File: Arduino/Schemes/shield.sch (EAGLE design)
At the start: 10 parts

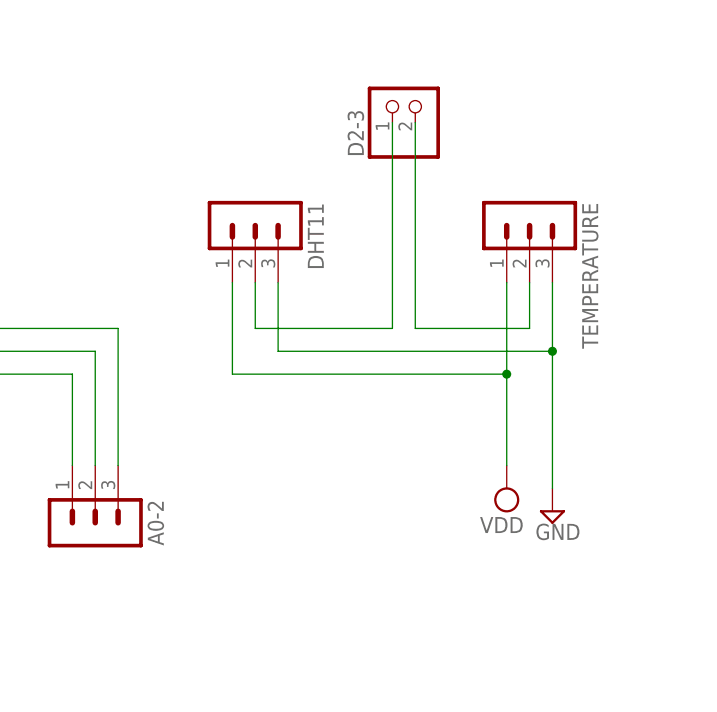
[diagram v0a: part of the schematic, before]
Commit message: relay board's scheme, shield with optional DHTxx
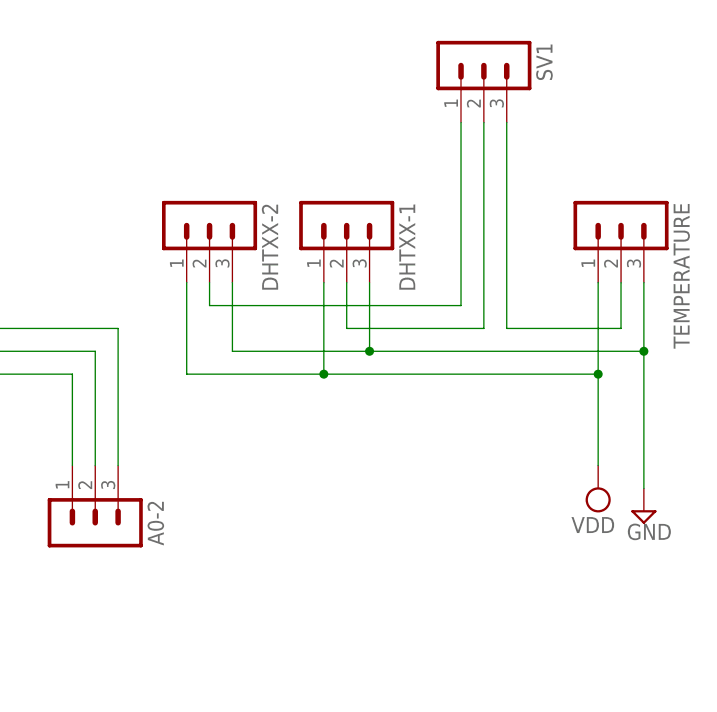
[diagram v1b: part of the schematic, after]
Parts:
- removed D2-3: (no value), pinhead:PINHD-1X2
- removed DHT11: (no value), con-lstb:MA03-1
- added DHTXX-1, DHTXX-2, SV1: (no value), con-lstb:MA03-1
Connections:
- new net N$9: DHTXX-2.2, SV1.1
- net GND: now also DHTXX-1.3, DHTXX-2.3; no longer DHT11.3
- net N$1: now also DHTXX-1.2, SV1.2; no longer D2-3.1, DHT11.2
- net N$2: now also SV1.3; no longer D2-3.2
- net VDD: now also DHTXX-1.1, DHTXX-2.1; no longer DHT11.1
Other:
- moved on the sheet: TEMPERATURE
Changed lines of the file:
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@@
 <part name="LIGHT" library="con-lstb" deviceset="MA03-1" device=""/>
 <part name="TEMPERATURE" library="con-lstb" deviceset="MA03-1" device=""/>
-<part name="DHT11" library="con-lstb" deviceset="MA03-1" device=""/>
+<part name="DHTXX-1" library="con-lstb" deviceset="MA03-1" device=""/>
 <part name="A0-2" library="con-lstb" deviceset="MA03-1" device=""/>
 <part name="5V-GND" library="pinhead" deviceset="PINHD-1X2" device=""/>
-<part name="D2-3" library="pinhead" deviceset="PINHD-1X2" device=""/>
 <part name="SUPPLY1" library="supply2" deviceset="GND" device=""/>
 <part name="SUPPLY2" library="supply2" deviceset="VDD" device=""/>
@@
 <part name="D8-10" library="con-lstb" deviceset="MA03-1" device=""/>
 <part name="RELAYS" library="con-lstb" deviceset="MA05-1" device=""/>
+<part name="SV1" library="con-lstb" deviceset="MA03-1" device=""/>
+<part name="DHTXX-2" library="con-lstb" deviceset="MA03-1" device=""/>
 </parts>
 <sheets>
@@
 <instance part="HUMIDITY2" gate="G$1" x="43.18" y="43.18" rot="R270"/>
 <instance part="LIGHT" gate="G$1" x="63.5" y="43.18" rot="R270"/>
-<instance part="TEMPERATURE" gate="G$1" x="139.7" y="40.64" rot="R270"/>
-<instance part="DHT11" gate="G$1" x="109.22" y="40.64" rot="R270"/>
+<instance part="TEMPERATURE" gate="G$1" x="149.86" y="40.64" rot="R270"/>
+<instance part="DHTXX-1" gate="G$1" x="119.38" y="40.64" rot="R270"/>
 <instance part="A0-2" gate="G$1" x="91.44" y="5.08" rot="MR90"/>
 <instance part="5V-GND" gate="G$1" x="25.4" y="-20.32" rot="R270"/>
-<instance part="D2-3" gate="G$1" x="127" y="53.34" rot="R90"/>
 <instance part="SUPPLY1" gate="GND" x="30.48" y="0" rot="R180"/>
 <instance part="SUPPLY2" gate="G$1" x="25.4" y="-5.08"/>
@@
 <instance part="SUPPLY6" gate="G$1" x="63.5" y="10.16" rot="R180"/>
 <instance part="SUPPLY7" gate="GND" x="60.96" y="12.7"/>
-<instance part="SUPPLY8" gate="GND" x="142.24" y="7.62"/>
-<instance part="SUPPLY9" gate="G$1" x="137.16" y="10.16" rot="R180"/>
+<instance part="SUPPLY8" gate="GND" x="152.4" y="7.62"/>
+<instance part="SUPPLY9" gate="G$1" x="147.32" y="10.16" rot="R180"/>
 <instance part="SUPPLY10" gate="GND" x="-15.24" y="20.32"/>
 <instance part="D8-10" gate="G$1" x="-2.54" y="60.96" rot="R270"/>
 <instance part="RELAYS" gate="G$1" x="-20.32" y="45.72" rot="R270"/>
+<instance part="SV1" gate="G$1" x="134.62" y="58.42" rot="R270"/>
+<instance part="DHTXX-2" gate="G$1" x="104.14" y="40.64" rot="R270"/>
 </instances>
 <busses>
@@
 <pinref part="TEMPERATURE" gate="G$1" pin="3"/>
 <pinref part="SUPPLY8" gate="GND" pin="GND"/>
-<wire x1="142.24" y1="33.02" x2="142.24" y2="25.4" width="0.1524" layer="91"/>
-<pinref part="DHT11" gate="G$1" pin="3"/>
-<wire x1="142.24" y1="25.4" x2="142.24" y2="10.16" width="0.1524" layer="91"/>
-<wire x1="111.76" y1="33.02" x2="111.76" y2="25.4" width="0.1524" layer="91"/>
-<wire x1="111.76" y1="25.4" x2="142.24" y2="25.4" width="0.1524" layer="91"/>
-<junction x="142.24" y="25.4"/>
+<wire x1="152.4" y1="33.02" x2="152.4" y2="25.4" width="0.1524" layer="91"/>
+<pinref part="DHTXX-1" gate="G$1" pin="3"/>
+<wire x1="152.4" y1="25.4" x2="152.4" y2="10.16" width="0.1524" layer="91"/>
+<wire x1="121.92" y1="33.02" x2="121.92" y2="25.4" width="0.1524" layer="91"/>
+<wire x1="121.92" y1="25.4" x2="152.4" y2="25.4" width="0.1524" layer="91"/>
+<junction x="152.4" y="25.4"/>
+<pinref part="DHTXX-2" gate="G$1" pin="3"/>
+<wire x1="121.92" y1="25.4" x2="106.68" y2="25.4" width="0.1524" layer="91"/>
+<wire x1="106.68" y1="25.4" x2="106.68" y2="33.02" width="0.1524" layer="91"/>
+<junction x="121.92" y="25.4"/>
 </segment>
 <segment>
@@
 <pinref part="TEMPERATURE" gate="G$1" pin="1"/>
 <pinref part="SUPPLY9" gate="G$1" pin="VDD"/>
-<wire x1="137.16" y1="33.02" x2="137.16" y2="22.86" width="0.1524" layer="91"/>
-<pinref part="DHT11" gate="G$1" pin="1"/>
-<wire x1="137.16" y1="22.86" x2="137.16" y2="12.7" width="0.1524" layer="91"/>
-<wire x1="106.68" y1="33.02" x2="106.68" y2="22.86" width="0.1524" layer="91"/>
-<wire x1="106.68" y1="22.86" x2="137.16" y2="22.86" width="0.1524" layer="91"/>
-<junction x="137.16" y="22.86"/>
+<wire x1="147.32" y1="33.02" x2="147.32" y2="22.86" width="0.1524" layer="91"/>
+<pinref part="DHTXX-1" gate="G$1" pin="1"/>
+<wire x1="147.32" y1="22.86" x2="147.32" y2="12.7" width="0.1524" layer="91"/>
+<wire x1="116.84" y1="33.02" x2="116.84" y2="22.86" width="0.1524" layer="91"/>
+<wire x1="116.84" y1="22.86" x2="147.32" y2="22.86" width="0.1524" layer="91"/>
+<junction x="147.32" y="22.86"/>
+<pinref part="DHTXX-2" gate="G$1" pin="1"/>
+<wire x1="116.84" y1="22.86" x2="101.6" y2="22.86" width="0.1524" layer="91"/>
+<wire x1="101.6" y1="22.86" x2="101.6" y2="33.02" width="0.1524" layer="91"/>
+<junction x="116.84" y="22.86"/>
 </segment>
 </net>
 <net name="N$1" class="0">
 <segment>
-<pinref part="DHT11" gate="G$1" pin="2"/>
-<wire x1="109.22" y1="33.02" x2="109.22" y2="27.94" width="0.1524" layer="91"/>
-<pinref part="D2-3" gate="G$1" pin="1"/>
-<wire x1="109.22" y1="27.94" x2="124.46" y2="27.94" width="0.1524" layer="91"/>
-<wire x1="124.46" y1="27.94" x2="124.46" y2="50.8" width="0.1524" layer="91"/>
+<pinref part="DHTXX-1" gate="G$1" pin="2"/>
+<wire x1="119.38" y1="33.02" x2="119.38" y2="27.94" width="0.1524" layer="91"/>
+<wire x1="119.38" y1="27.94" x2="134.62" y2="27.94" width="0.1524" layer="91"/>
+<wire x1="134.62" y1="27.94" x2="134.62" y2="50.8" width="0.1524" layer="91"/>
+<pinref part="SV1" gate="G$1" pin="2"/>
 </segment>
 </net>
 <net name="N$2" class="0">
 <segment>
-<pinref part="D2-3" gate="G$1" pin="2"/>
-<wire x1="127" y1="50.8" x2="127" y2="27.94" width="0.1524" layer="91"/>
 <pinref part="TEMPERATURE" gate="G$1" pin="2"/>
-<wire x1="127" y1="27.94" x2="139.7" y2="27.94" width="0.1524" layer="91"/>
-<wire x1="139.7" y1="27.94" x2="139.7" y2="33.02" width="0.1524" layer="91"/>
+<wire x1="137.16" y1="50.8" x2="137.16" y2="27.94" width="0.1524" layer="91"/>
+<wire x1="137.16" y1="27.94" x2="149.86" y2="27.94" width="0.1524" layer="91"/>
+<wire x1="149.86" y1="27.94" x2="149.86" y2="33.02" width="0.1524" layer="91"/>
+<pinref part="SV1" gate="G$1" pin="3"/>
 </segment>
 </net>
@@
 </segment>
 </net>
+<net name="N$9" class="0">
+<segment>
+<pinref part="SV1" gate="G$1" pin="1"/>
+<wire x1="132.08" y1="50.8" x2="132.08" y2="30.48" width="0.1524" layer="91"/>
+<pinref part="DHTXX-2" gate="G$1" pin="2"/>
+<wire x1="132.08" y1="30.48" x2="104.14" y2="30.48" width="0.1524" layer="91"/>
+<wire x1="104.14" y1="30.48" x2="104.14" y2="33.02" width="0.1524" layer="91"/>
+</segment>
+</net>
